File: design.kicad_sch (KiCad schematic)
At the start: 19 parts, among them J1 Conn_02x02_Counter_Clockwise, J2 Conn_02x02_Counter_Clockwise, J3 Conn_02x02_Counter_Clockwise, U1 TPS63900

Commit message: update
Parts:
- added J?: Conn_02x02_Counter_Clockwise, Connector_PinSocket_2.54mm:PinSocket_2x02_P2.54mm_Vertical, symbol Connector_Generic:Conn_02x02_Counter_Clockwise
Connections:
- net GND: now also J?.3 (Pin_3), J?.4 (Pin_4)
- net SEL: now also J2.1 (Pin_1); no longer J2.2 (Pin_2)
- net Vin: now also J1.4 (Pin_4), J2.2 (Pin_2), J?.1 (Pin_1), J?.2 (Pin_2); no longer J1.1 (Pin_1), J2.1 (Pin_1)
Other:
- moved on the sheet: J1, J2

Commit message: update
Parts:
- TP1, TP3, TP5, TP6, TP7: value TestPoint -> GND
- TP2: value TestPoint -> Vin
- TP4: value TestPoint -> Vout
- gave numbers to parts that had none: 1
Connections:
- net GND: now also J1.1 (Pin_1), R1.1, R3.1; no longer J1.3 (Pin_3)

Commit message: update
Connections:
- net GND: now also J2.1 (Pin_1), J3.1 (Pin_1), J4.1 (Pin_1); no longer J2.3 (Pin_3), J3.4 (Pin_4), J4.4 (Pin_4)
- net SEL: now also J2.2 (Pin_2); no longer J2.1 (Pin_1)
- net Vin: now also J2.4 (Pin_4), J4.4 (Pin_4); no longer J2.2 (Pin_2), J4.1 (Pin_1)
- net Vout: now also J3.4 (Pin_4); no longer J3.1 (Pin_1)
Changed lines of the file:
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@@
     (comment 4 "<<hash>>")
   )
-  (junction (at 85.09 99.06) (diameter 0) (color 0 0 0 0)
-  )
   (junction (at 247.65 66.04) (diameter 0) (color 0 0 0 0)
   )
@@
   (junction (at 177.8 111.76) (diameter 0) (color 0 0 0 0)
   )
-  (junction (at 205.74 66.04) (diameter 0) (color 0 0 0 0)
-  )
   (junction (at 177.8 114.3) (diameter 0) (color 0 0 0 0)
   )
   (no_connect (at 132.08 144.78))
-  (no_connect (at 177.8 142.24))
+  (no_connect (at 177.8 144.78))
   (wire (pts (xy 251.46 63.5) (xy 251.46 66.04))
     (stroke (width 0) (type default) (color 0 0 0 0))
@@
     (stroke (width 0) (type default) (color 0 0 0 0))
   )
+  (wire (pts (xy 156.845 142.24) (xy 165.1 142.24))
+    (stroke (width 0) (type default) (color 0 0 0 0))
+  )
   (wire (pts (xy 236.22 63.5) (xy 236.22 66.04))
     (stroke (width 0) (type default) (color 0 0 0 0))
@@
     (stroke (width 0) (type default) (color 0 0 0 0))
   )
+  (wire (pts (xy 156.845 145.415) (xy 156.845 142.24))
+    (stroke (width 0) (type default) (color 0 0 0 0))
+  )
   (wire (pts (xy 195.58 91.44) (xy 195.58 96.52))
     (stroke (width 0) (type default) (color 0 0 0 0))
   )
+  (wire (pts (xy 60.96 96.52) (xy 69.85 96.52))
+    (stroke (width 0) (type default) (color 0 0 0 0))
+  )
   (wire (pts (xy 259.08 63.5) (xy 259.08 66.04))
     (stroke (width 0) (type default) (color 0 0 0 0))
   )
+  (wire (pts (xy 180.34 63.5) (xy 190.5 63.5))
+    (stroke (width 0) (type default) (color 0 0 0 0))
+  )
   (wire (pts (xy 157.48 101.6) (xy 160.02 101.6))
     (stroke (width 0) (type default) (color 0 0 0 0))
@@
     (stroke (width 0) (type default) (color 0 0 0 0))
   )
-  (wire (pts (xy 177.8 144.78) (xy 180.34 144.78))
-    (stroke (width 0) (type default) (color 0 0 0 0))
-  )
-  (wire (pts (xy 85.09 96.52) (xy 85.09 99.06))
-    (stroke (width 0) (type default) (color 0 0 0 0))
-  )
   (wire (pts (xy 251.46 66.04) (xy 247.65 66.04))
     (stroke (width 0) (type default) (color 0 0 0 0))
   )
-  (wire (pts (xy 205.74 63.5) (xy 205.74 66.04))
-    (stroke (width 0) (type default) (color 0 0 0 0))
-  )
   (wire (pts (xy 157.48 99.06) (xy 170.18 99.06))
     (stroke (width 0) (type default) (color 0 0 0 0))
   )
-  (wire (pts (xy 203.2 66.04) (xy 205.74 66.04))
-    (stroke (width 0) (type default) (color 0 0 0 0))
-  )
-  (wire (pts (xy 85.09 99.06) (xy 87.63 99.06))
-    (stroke (width 0) (type default) (color 0 0 0 0))
-  )
   (wire (pts (xy 247.65 66.04) (xy 247.65 71.12))
     (stroke (width 0) (type default) (color 0 0 0 0))
@@
     (stroke (width 0) (type default) (color 0 0 0 0))
   )
+  (wire (pts (xy 60.96 99.06) (xy 60.96 96.52))
+    (stroke (width 0) (type default) (color 0 0 0 0))
+  )
   (wire (pts (xy 228.6 63.5) (xy 228.6 66.04))
     (stroke (width 0) (type default) (color 0 0 0 0))
@@
     (stroke (width 0) (type default) (color 0 0 0 0))
   )
-  (wire (pts (xy 82.55 96.52) (xy 85.09 96.52))
-    (stroke (width 0) (type default) (color 0 0 0 0))
-  )
   (wire (pts (xy 167.64 111.76) (xy 177.8 111.76))
     (stroke (width 0) (type default) (color 0 0 0 0))
   )
-  (wire (pts (xy 203.2 63.5) (xy 205.74 63.5))
-    (stroke (width 0) (type default) (color 0 0 0 0))
-  )
-  (wire (pts (xy 82.55 99.06) (xy 85.09 99.06))
+  (wire (pts (xy 82.55 99.06) (xy 87.63 99.06))
     (stroke (width 0) (type default) (color 0 0 0 0))
   )
@@
     (stroke (width 0) (type default) (color 0 0 0 0))
   )
-  (wire (pts (xy 205.74 66.04) (xy 208.28 66.04))
+  (wire (pts (xy 203.2 66.04) (xy 208.28 66.04))
+    (stroke (width 0) (type default) (color 0 0 0 0))
+  )
+  (wire (pts (xy 180.34 66.04) (xy 180.34 63.5))
     (stroke (width 0) (type default) (color 0 0 0 0))
   )
@@
     )
   )
-  (global_label "SEL" (shape input) (at 165.1 142.24 180) (fields_autoplaced)
-    (effects (font (size 1.27 1.27)) (justify right))
-    (property "Referenzen zwischen Schaltplänen" "${INTERSHEET_REFS}" (id 0) (at 159.3891 142.1606 0)
+  (global_label "SEL" (shape input) (at 165.1 144.78 180) (fields_autoplaced)
+    (effects (font (size 1.27 1.27)) (justify right))
+    (property "Referenzen zwischen Schaltplänen" "${INTERSHEET_REFS}" (id 0) (at 159.3891 144.7006 0)
       (effects (font (size 1.27 1.27)) (justify right) hide)
     )
@@
     )
   )
-  (global_label "Vout" (shape input) (at 190.5 63.5 180) (fields_autoplaced)
-    (effects (font (size 1.27 1.27)) (justify right))
-    (property "Referenzen zwischen Schaltplänen" "${INTERSHEET_REFS}" (id 0) (at 184.0634 63.5794 0)
-      (effects (font (size 1.27 1.27)) (justify right) hide)
+  (global_label "Vout" (shape input) (at 203.2 63.5 0) (fields_autoplaced)
+    (effects (font (size 1.27 1.27)) (justify left))
+    (property "Referenzen zwischen Schaltplänen" "${INTERSHEET_REFS}" (id 0) (at 209.6366 63.4206 0)
+      (effects (font (size 1.27 1.27)) (justify left) hide)
     )
   )
@@
     )
   )
-  (global_label "Vin" (shape input) (at 69.85 96.52 180) (fields_autoplaced)
-    (effects (font (size 1.27 1.27)) (justify right))
-    (property "Referenzen zwischen Schaltplänen" "${INTERSHEET_REFS}" (id 0) (at 64.6834 96.4406 0)
-      (effects (font (size 1.27 1.27)) (justify right) hide)
+  (global_label "Vin" (shape input) (at 82.55 96.52 0) (fields_autoplaced)
+    (effects (font (size 1.27 1.27)) (justify left))
+    (property "Referenzen zwischen Schaltplänen" "${INTERSHEET_REFS}" (id 0) (at 87.7166 96.5994 0)
+      (effects (font (size 1.27 1.27)) (justify left) hide)
     )
   )
@@
     )
   )
-  (global_label "Vin" (shape input) (at 165.1 144.78 180) (fields_autoplaced)
-    (effects (font (size 1.27 1.27)) (justify right))
-    (property "Referenzen zwischen Schaltplänen" "${INTERSHEET_REFS}" (id 0) (at 159.9334 144.8594 0)
-      (effects (font (size 1.27 1.27)) (justify right) hide)
+  (global_label "Vin" (shape input) (at 177.8 142.24 0) (fields_autoplaced)
+    (effects (font (size 1.27 1.27)) (justify left))
+    (property "Referenzen zwischen Schaltplänen" "${INTERSHEET_REFS}" (id 0) (at 182.9666 142.1606 0)
+      (effects (font (size 1.27 1.27)) (justify left) hide)
     )
   )
@@
     (pin "1")
   )
-  (symbol (lib_id "power:GND") (at 180.34 144.78 0) (unit 1)
-    (in_bom yes) (on_board yes) (fields_autoplaced)
-    (property "Reference" "#PWR0103" (id 0) (at 180.34 151.13 0)
-      (effects (font (size 1.27 1.27)) hide)
-    )
-    (property "Value" "GND" (id 1) (at 180.34 149.86 0))
-    (property "Footprint" "" (id 2) (at 180.34 144.78 0)
-      (effects (font (size 1.27 1.27)) hide)
-    )
-    (property "Datasheet" "" (id 3) (at 180.34 144.78 0)
+  (symbol (lib_id "power:GND") (at 156.845 145.415 0) (unit 1)
+    (in_bom yes) (on_board yes) (fields_autoplaced)
+    (property "Reference" "#PWR0103" (id 0) (at 156.845 151.765 0)
+      (effects (font (size 1.27 1.27)) hide)
+    )
+    (property "Value" "GND" (id 1) (at 156.845 150.495 0))
+    (property "Footprint" "" (id 2) (at 156.845 145.415 0)
+      (effects (font (size 1.27 1.27)) hide)
+    )
+    (property "Datasheet" "" (id 3) (at 156.845 145.415 0)
       (effects (font (size 1.27 1.27)) hide)
     )
@@
     )
     (property "Datasheet" "" (id 3) (at 147.32 116.84 0)
+      (effects (font (size 1.27 1.27)) hide)
+    )
+    (pin "1")
+  )
+  (symbol (lib_id "power:GND") (at 60.96 99.06 0) (unit 1)
+    (in_bom yes) (on_board yes) (fields_autoplaced)
+    (property "Reference" "#PWR0112" (id 0) (at 60.96 105.41 0)
+      (effects (font (size 1.27 1.27)) hide)
+    )
+    (property "Value" "GND" (id 1) (at 60.96 104.14 0))
+    (property "Footprint" "" (id 2) (at 60.96 99.06 0)
+      (effects (font (size 1.27 1.27)) hide)
+    )
+    (property "Datasheet" "" (id 3) (at 60.96 99.06 0)
       (effects (font (size 1.27 1.27)) hide)
     )
@@
     (pin "1")
   )
+  (symbol (lib_id "power:GND") (at 180.34 66.04 0) (unit 1)
+    (in_bom yes) (on_board yes) (fields_autoplaced)
+    (property "Reference" "#PWR0111" (id 0) (at 180.34 72.39 0)
+      (effects (font (size 1.27 1.27)) hide)
+    )
+    (property "Value" "GND" (id 1) (at 180.34 71.12 0))
+    (property "Footprint" "" (id 2) (at 180.34 66.04 0)
+      (effects (font (size 1.27 1.27)) hide)
+    )
+    (property "Datasheet" "" (id 3) (at 180.34 66.04 0)
+      (effects (font (size 1.27 1.27)) hide)
+    )
+    (pin "1")
+  )
   (symbol (lib_id "Snapeda:RCWCTE") (at 228.6 114.3 90) (unit 1)
     (in_bom yes) (on_board yes) (fields_autoplaced)
@@
       (reference "#PWR0110") (unit 1) (value "GND") (footprint "")
     )
+    (path "/e644cbf8-44e3-4e52-8bfb-67e5d91dff4d"
+      (reference "#PWR0111") (unit 1) (value "GND") (footprint "")
+    )
+    (path "/425ffa30-1c7d-42ae-981f-4a3a2abd9b6c"
+      (reference "#PWR0112") (unit 1) (value "GND") (footprint "")
+    )
     (path "/5597932a-9308-4b20-96c5-01a9581bd15c"

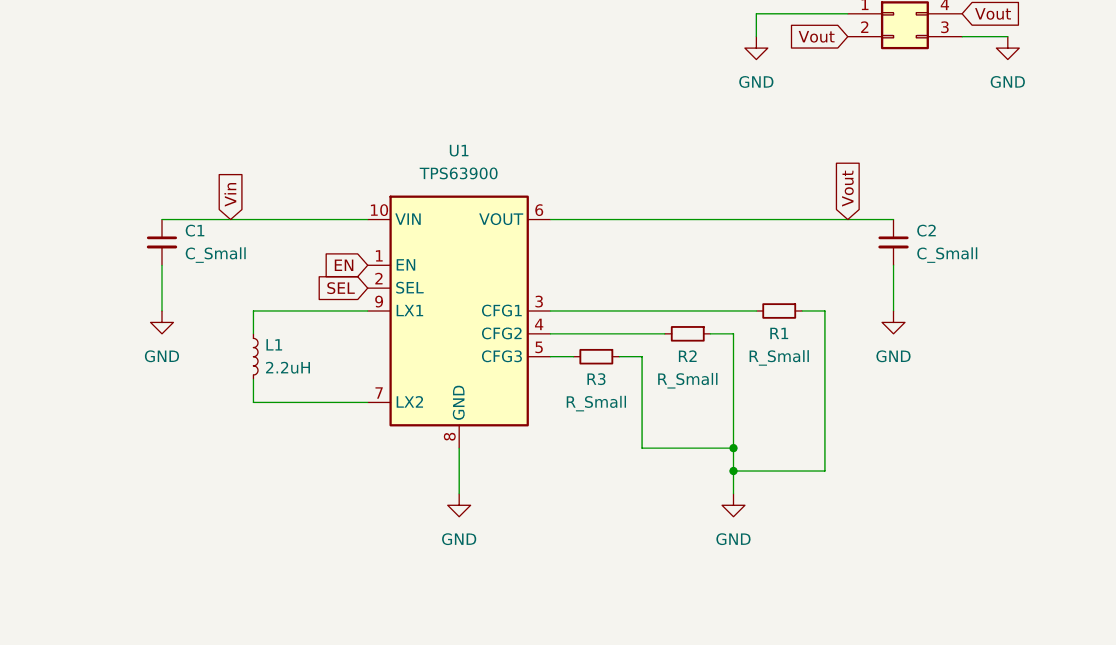
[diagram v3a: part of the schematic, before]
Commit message: add power flags
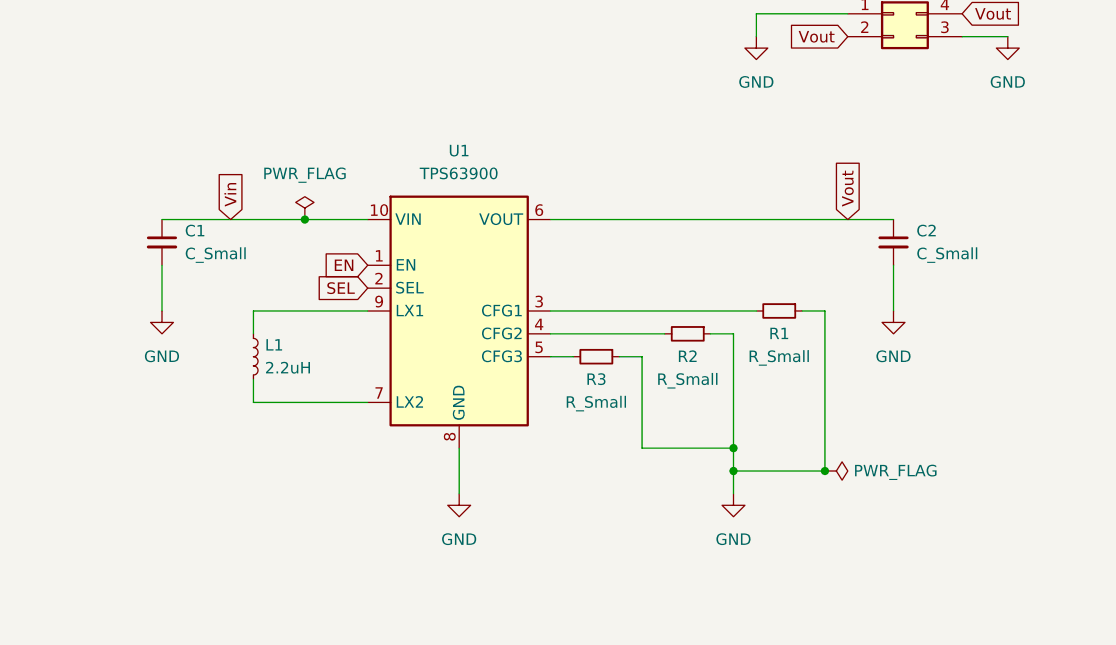
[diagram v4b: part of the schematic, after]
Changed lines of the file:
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@@
   (junction (at 177.8 111.76) (diameter 0) (color 0 0 0 0)
   )
+  (junction (at 130.175 86.36) (diameter 0) (color 0 0 0 0)
+  )
   (junction (at 177.8 114.3) (diameter 0) (color 0 0 0 0)
+  )
+  (junction (at 187.96 114.3) (diameter 0) (color 0 0 0 0)
   )
   (no_connect (at 132.08 144.78))
@@
     (stroke (width 0) (type default) (color 0 0 0 0))
   )
-  (wire (pts (xy 114.3 86.36) (xy 137.16 86.36))
+  (wire (pts (xy 114.3 86.36) (xy 130.175 86.36))
     (stroke (width 0) (type default) (color 0 0 0 0))
   )
@@
   )
   (wire (pts (xy 157.48 101.6) (xy 160.02 101.6))
+    (stroke (width 0) (type default) (color 0 0 0 0))
+  )
+  (wire (pts (xy 130.175 86.36) (xy 137.16 86.36))
     (stroke (width 0) (type default) (color 0 0 0 0))
   )
@@
     (pin "3")
     (pin "4")
+  )
+  (symbol (lib_id "power:PWR_FLAG") (at 187.96 114.3 270) (unit 1)
+    (in_bom yes) (on_board yes) (fields_autoplaced)
+    (property "Reference" "#FLG0102" (id 0) (at 189.865 114.3 0)
+      (effects (font (size 1.27 1.27)) hide)
+    )
+    (property "Value" "PWR_FLAG" (id 1) (at 191.135 114.2999 90)
+      (effects (font (size 1.27 1.27)) (justify left))
+    )
+    (property "Footprint" "" (id 2) (at 187.96 114.3 0)
+      (effects (font (size 1.27 1.27)) hide)
+    )
+    (property "Datasheet" "~" (id 3) (at 187.96 114.3 0)
+      (effects (font (size 1.27 1.27)) hide)
+    )
+    (pin "1")
   )
   (symbol (lib_id "Device:C_Small") (at 114.3 88.9 0) (unit 1)
@@
     (pin "1")
   )
+  (symbol (lib_id "power:PWR_FLAG") (at 130.175 86.36 0) (unit 1)
+    (in_bom yes) (on_board yes) (fields_autoplaced)
+    (property "Reference" "#FLG0101" (id 0) (at 130.175 84.455 0)
+      (effects (font (size 1.27 1.27)) hide)
+    )
+    (property "Value" "PWR_FLAG" (id 1) (at 130.175 81.28 0))
+    (property "Footprint" "" (id 2) (at 130.175 86.36 0)
+      (effects (font (size 1.27 1.27)) hide)
+    )
+    (property "Datasheet" "~" (id 3) (at 130.175 86.36 0)
+      (effects (font (size 1.27 1.27)) hide)
+    )
+    (pin "1")
+  )
   (symbol (lib_id "power:GND") (at 180.34 66.04 0) (unit 1)
     (in_bom yes) (on_board yes) (fields_autoplaced)
@@
   )
   (symbol_instances
+    (path "/e1095be5-de1a-462e-a8d7-6fa0e5884d0c"
+      (reference "#FLG0101") (unit 1) (value "PWR_FLAG") (footprint "")
+    )
+    (path "/4e68fbeb-ae47-4bdd-8961-4217c26523ad"
+      (reference "#FLG0102") (unit 1) (value "PWR_FLAG") (footprint "")
+    )
     (path "/9fe5fea7-bad8-4113-a38a-5acb21ddc01c"
       (reference "#PWR0101") (unit 1) (value "GND") (footprint "")
